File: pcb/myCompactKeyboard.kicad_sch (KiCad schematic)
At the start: 290 parts, among them J1 OLED_128x64, SW1 RotaryEncoder_Switch, SW2 RotaryEncoder_Switch, U1 Raspberry_Pi_Pico

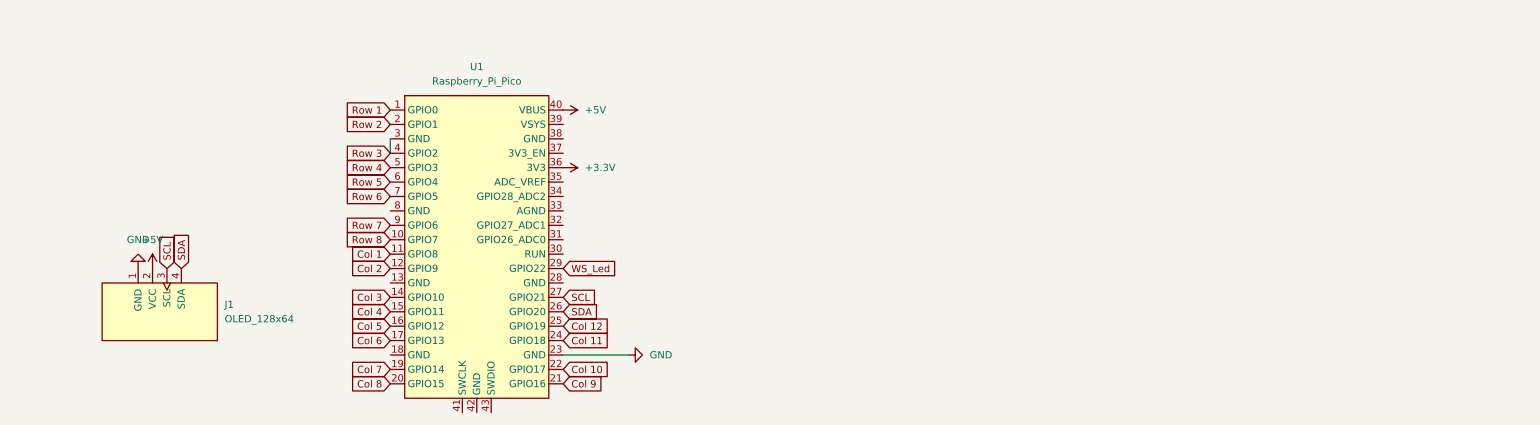
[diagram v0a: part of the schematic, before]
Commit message: added a jack conector
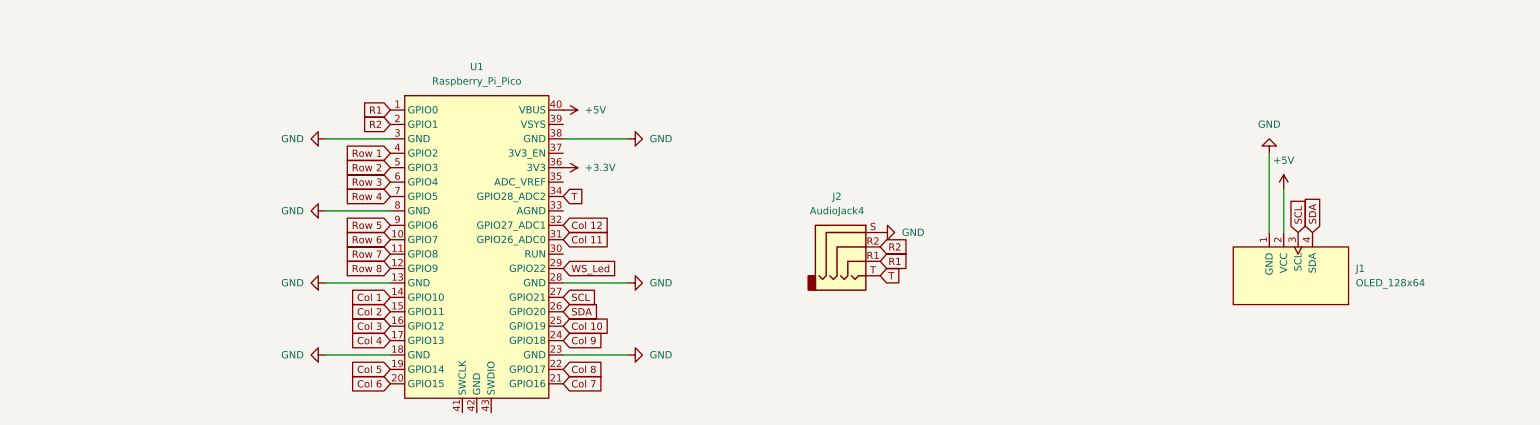
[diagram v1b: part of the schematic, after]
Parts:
- added J2: AudioJack4, symbol Connector_Audio:AudioJack4
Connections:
- net Col 1: now also U1.14 (GPIO10); no longer U1.11 (GPIO8)
- net Col 10: now also U1.25 (GPIO19); no longer U1.22 (GPIO17)
- net Col 11: now also U1.31 (GPIO26_ADC0); no longer U1.24 (GPIO18)
- net Col 12: now also U1.32 (GPIO27_ADC1); no longer U1.25 (GPIO19)
- net Col 2: now also U1.15 (GPIO11); no longer U1.12 (GPIO9)
- net Col 3: now also U1.16 (GPIO12); no longer U1.14 (GPIO10)
- net Col 4: now also U1.17 (GPIO13); no longer U1.15 (GPIO11)
- net Col 5: now also U1.19 (GPIO14); no longer U1.16 (GPIO12)
- net Col 6: now also U1.20 (GPIO15); no longer U1.17 (GPIO13)
- net Col 7: now also U1.21 (GPIO16); no longer U1.19 (GPIO14)
- net Col 8: now also U1.22 (GPIO17); no longer U1.20 (GPIO15)
- net Col 9: now also U1.24 (GPIO18); no longer U1.21 (GPIO16)
- net GND: now also U1.13 (GND), U1.18 (GND), U1.28 (GND), U1.3 (GND), U1.38 (GND), U1.8 (GND), J2.S
- net Row 1: now also U1.4 (GPIO2); no longer U1.1 (GPIO0)
- net Row 2: now also U1.5 (GPIO3); no longer U1.2 (GPIO1)
- net Row 3: now also U1.6 (GPIO4); no longer U1.3 (GND), U1.4 (GPIO2)
- net Row 4: now also U1.7 (GPIO5); no longer U1.5 (GPIO3)
- net Row 5: now also U1.9 (GPIO6); no longer U1.6 (GPIO4)
- net Row 6: now also U1.10 (GPIO7); no longer U1.7 (GPIO5)
- net Row 7: now also U1.11 (GPIO8); no longer U1.9 (GPIO6)
- net Row 8: now also U1.12 (GPIO9); no longer U1.10 (GPIO7)
- net T: now reaches U1.34 (GPIO28_ADC2)
- net T: now also J2.T
- new net R1: J2.R1, U1.1 (GPIO0)
- new net R2: J2.R2, U1.2 (GPIO1)
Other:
- moved on the sheet: J1

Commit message: wired all simple keyswitch connections
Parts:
- J2: footprint (none) -> Connector_Audio:Jack_3.5mm_CUI_SJ1-3524N_Horizontal
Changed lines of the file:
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@@
 			)
 		)
-		(property "Footprint" ""
+		(property "Footprint" "Connector_Audio:Jack_3.5mm_CUI_SJ1-3524N_Horizontal"
 			(at 227.33 308.61 0)
 			(effects

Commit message: changed jack to smd and fixed all errors and many warnings
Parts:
- J2: footprint Connector_Audio:Jack_3.5mm_CUI_SJ1-3524N_Horizontal -> Connector_Audio:Jack_3.5mm_CUI_SJ-3524-SMT_Horizontal
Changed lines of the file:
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@@
 			)
 		)
-		(property "Footprint" "Connector_Audio:Jack_3.5mm_CUI_SJ1-3524N_Horizontal"
+		(property "Footprint" "Connector_Audio:Jack_3.5mm_CUI_SJ-3524-SMT_Horizontal"
 			(at 227.33 308.61 0)
 			(effects

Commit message: added x.00u switches (instead of 1.00)
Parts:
- S54, S55: footprint ScottoKeebs_MX:MX_PCB_1.00u -> ScottoKeebs_MX:MX_PCB_3.00u
- S80: footprint ScottoKeebs_MX:MX_PCB_1.00u -> ScottoKeebs_MX:MX_PCB_2.00u_90deg
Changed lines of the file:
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@@
 			)
 		)
-		(property "Footprint" "ScottoKeebs_MX:MX_PCB_1.00u"
+		(property "Footprint" "ScottoKeebs_MX:MX_PCB_2.00u_90deg"
 			(at 129.54 231.14 0)
 			(effects
@@
 			)
 		)
-		(property "Footprint" "ScottoKeebs_MX:MX_PCB_1.00u"
+		(property "Footprint" "ScottoKeebs_MX:MX_PCB_3.00u"
 			(at 53.34 205.74 0)
 			(effects
@@
 			)
 		)
-		(property "Footprint" "ScottoKeebs_MX:MX_PCB_1.00u"
+		(property "Footprint" "ScottoKeebs_MX:MX_PCB_3.00u"
 			(at 53.34 180.34 0)
 			(effects

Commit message: moved half a row down top keys
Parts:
- S54, S55: footprint ScottoKeebs_MX:MX_PCB_3.00u -> ScottoKeebs_Scotto:MX_Hotswap_3.00u
- S80: footprint ScottoKeebs_MX:MX_PCB_2.00u_90deg -> ScottoKeebs_Scotto:MX_Hotswap_2.00u
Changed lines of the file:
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@@
 			)
 		)
-		(property "Footprint" "ScottoKeebs_MX:MX_PCB_2.00u_90deg"
+		(property "Footprint" "ScottoKeebs_Scotto:MX_Hotswap_2.00u"
 			(at 129.54 231.14 0)
 			(effects
@@
 			)
 		)
-		(property "Footprint" "ScottoKeebs_MX:MX_PCB_3.00u"
+		(property "Footprint" "ScottoKeebs_Scotto:MX_Hotswap_3.00u"
 			(at 53.34 205.74 0)
 			(effects
@@
 			)
 		)
-		(property "Footprint" "ScottoKeebs_MX:MX_PCB_3.00u"
+		(property "Footprint" "ScottoKeebs_Scotto:MX_Hotswap_3.00u"
 			(at 53.34 180.34 0)
 			(effects

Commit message: fixed hotswap keys and jack
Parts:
- S80: footprint ScottoKeebs_Scotto:MX_Hotswap_2.00u -> ScottoKeebs_Hotswap:Hotswap_MX_2.00u_90deg
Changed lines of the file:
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@@
 			)
 		)
-		(property "Footprint" "ScottoKeebs_Scotto:MX_Hotswap_2.00u"
+		(property "Footprint" "ScottoKeebs_Hotswap:Hotswap_MX_2.00u_90deg"
 			(at 129.54 231.14 0)
 			(effects

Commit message: converted firs spacebar to 2.75u and alt to 1.25u
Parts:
- S55: footprint ScottoKeebs_Scotto:MX_Hotswap_3.00u -> ScottoKeebs_Scotto:MX_Hotswap_2.75u
- S63: footprint ScottoKeebs_MX:MX_PCB_1.00u -> ScottoKeebs_MX:MX_PCB_1.25u
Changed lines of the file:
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@@
 			)
 		)
-		(property "Footprint" "ScottoKeebs_MX:MX_PCB_1.00u"
+		(property "Footprint" "ScottoKeebs_MX:MX_PCB_1.25u"
 			(at 78.74 205.74 0)
 			(effects
@@
 			)
 		)
-		(property "Footprint" "ScottoKeebs_Scotto:MX_Hotswap_3.00u"
+		(property "Footprint" "ScottoKeebs_Scotto:MX_Hotswap_2.75u"
 			(at 53.34 205.74 0)
 			(effects

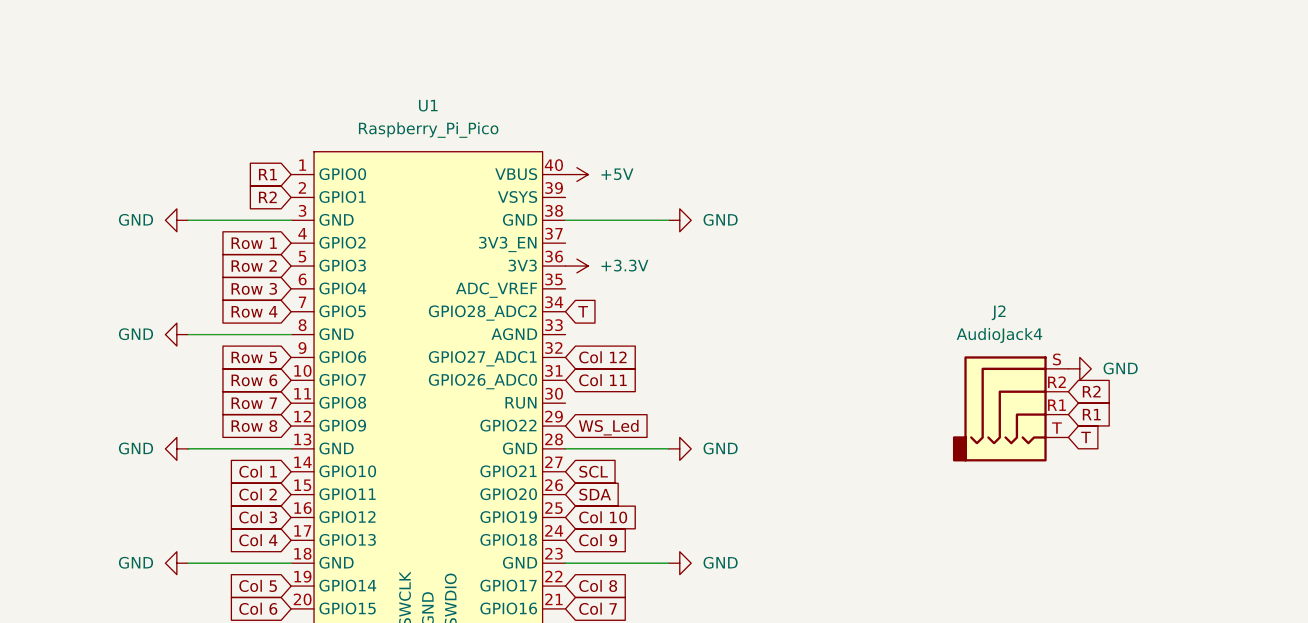
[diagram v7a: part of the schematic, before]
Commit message: remove jack and wire rotary encoders
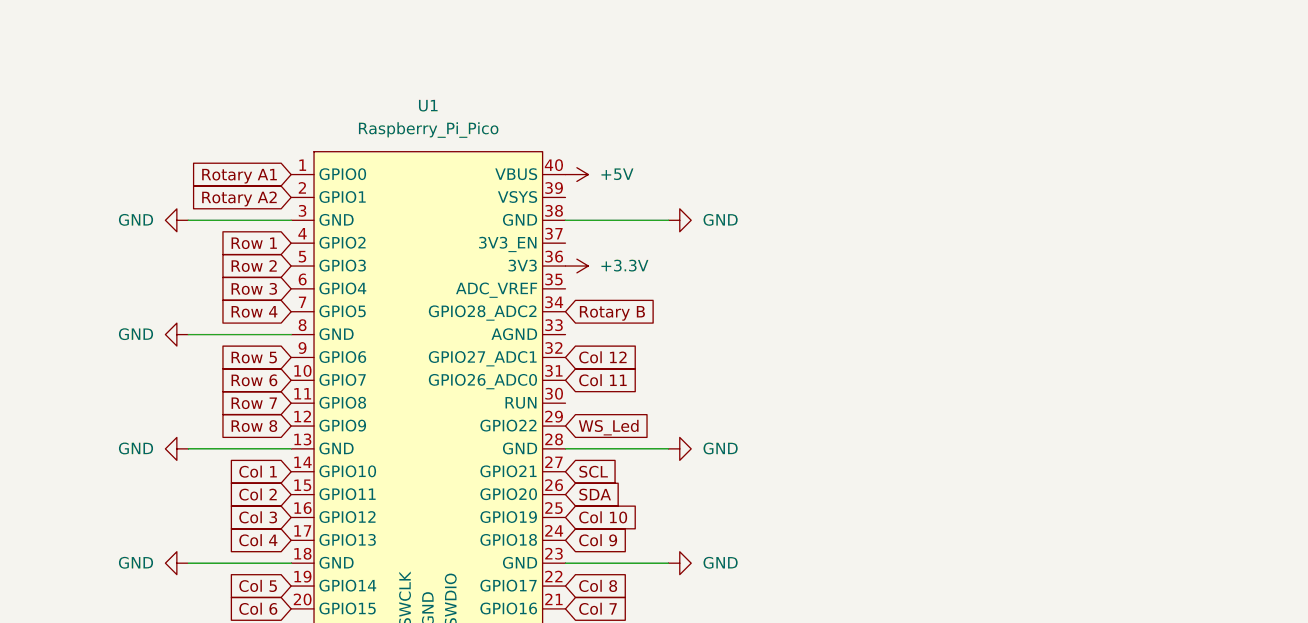
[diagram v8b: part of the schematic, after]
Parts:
- removed J2: AudioJack4, Connector_Audio:Jack_3.5mm_CUI_SJ-3524-SMT_Horizontal, symbol Connector_Audio:AudioJack4
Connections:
- net R1 is gone; now on net Rotary A1: U1.1 (GPIO0)
- net R2 is gone; now on net Rotary A2: U1.2 (GPIO1)
- net T is gone; now on net Rotary B: U1.34 (GPIO28_ADC2)
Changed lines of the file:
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@@
 		)
 	)
-	(global_label "T"
-		(shape input)
-		(at 232.41 313.69 0)
-		(fields_autoplaced yes)
-		(effects
-			(font
-				(size 1.27 1.27)
-			)
-			(justify left)
-		)
-		(property "Intersheetrefs" "${INTERSHEET_REFS}"
-			(at 236.3628 313.69 0)
-			(effects
-				(font
-					(size 1.27 1.27)
-				)
-				(justify left)
-				(hide yes)
-			)
-		)
-	)
-	(global_label "R1"
-		(shape input)
-		(at 146.05 284.48 180)
-		(fields_autoplaced yes)
-		(effects
-			(font
-				(size 1.27 1.27)
-			)
-			(justify right)
-		)
-		(property "Intersheetrefs" "${INTERSHEET_REFS}"
-			(at 140.5853 284.48 0)
-			(effects
-				(font
-					(size 1.27 1.27)
-				)
-				(justify right)
-				(hide yes)
-			)
-		)
-	)
 	(global_label "Col 8"
 		(shape input)
@@
 		)
 	)
-	(global_label "R2"
-		(shape input)
-		(at 146.05 287.02 180)
-		(fields_autoplaced yes)
-		(effects
-			(font
-				(size 1.27 1.27)
-			)
-			(justify right)
-		)
-		(property "Intersheetrefs" "${INTERSHEET_REFS}"
-			(at 140.5853 287.02 0)
-			(effects
-				(font
-					(size 1.27 1.27)
-				)
-				(justify right)
-				(hide yes)
-			)
-		)
-	)
 	(global_label "Col 1"
 		(shape input)
@@
 		)
 	)
-	(global_label "R2"
+	(global_label "Rotary A1"
 		(shape input)
-		(at 232.41 308.61 0)
+		(at 146.05 284.48 180)
 		(fields_autoplaced yes)
 		(effects
@@
 				(size 1.27 1.27)
 			)
-			(justify left)
+			(justify right)
 		)
 		(property "Intersheetrefs" "${INTERSHEET_REFS}"
-			(at 237.8747 308.61 0)
+			(at 133.7516 284.48 0)
 			(effects
 				(font
 					(size 1.27 1.27)
 				)
-				(justify left)
+				(justify right)
 				(hide yes)
 			)
@@
 		)
 	)
+	(global_label "Rotary A2"
+		(shape input)
+		(at 146.05 287.02 180)
+		(fields_autoplaced yes)
+		(effects
+			(font
+				(size 1.27 1.27)
+			)
+			(justify right)
+		)
+		(property "Intersheetrefs" "${INTERSHEET_REFS}"
+			(at 133.7516 287.02 0)
+			(effects
+				(font
+					(size 1.27 1.27)
+				)
+				(justify right)
+				(hide yes)
+			)
+		)
+	)
 	(global_label "Col 8"
 		(shape input)
@@
 		)
 	)
-	(global_label "T"
+	(global_label "WS_Led"
 		(shape input)
-		(at 176.53 299.72 0)
+		(at 276.86 25.4 180)
 		(fields_autoplaced yes)
 		(effects
@@
 				(size 1.27 1.27)
 			)
-			(justify left)
+			(justify right)
 		)
 		(property "Intersheetrefs" "${INTERSHEET_REFS}"
-			(at 180.4828 299.72 0)
+			(at 266.9806 25.4 0)
 			(effects
 				(font
 					(size 1.27 1.27)
 				)
-				(justify left)
+				(justify right)
 				(hide yes)
 			)
 		)
 	)
-	(global_label "WS_Led"
+	(global_label "Rotary B"
 		(shape input)
-		(at 276.86 25.4 180)
+		(at 176.53 299.72 0)
 		(fields_autoplaced yes)
 		(effects
@@
 				(size 1.27 1.27)
 			)
-			(justify right)
+			(justify left)
 		)
 		(property "Intersheetrefs" "${INTERSHEET_REFS}"
-			(at 266.9806 25.4 0)
+			(at 187.8003 299.72 0)
 			(effects
 				(font
 					(size 1.27 1.27)
 				)
-				(justify right)
+				(justify left)
 				(hide yes)
 			)
@@
 		)
 	)
-	(global_label "R1"
-		(shape input)
-		(at 232.41 311.15 0)
-		(fields_autoplaced yes)
-		(effects
-			(font
-				(size 1.27 1.27)
-			)
-			(justify left)
-		)
-		(property "Intersheetrefs" "${INTERSHEET_REFS}"
-			(at 237.8747 311.15 0)
-			(effects
-				(font
-					(size 1.27 1.27)
-				)
-				(justify left)
-				(hide yes)
-			)
-		)
-	)
 	(global_label "Row 4"
 		(shape input)
@@
 	)
 	(symbol
-		(lib_id "power:GND")
-		(at 232.41 306.07 90)
-		(unit 1)
-		(exclude_from_sim no)
-		(in_bom yes)
-		(on_board yes)
-		(dnp no)
-		(fields_autoplaced yes)
-		(property "Reference" "#PWR012"
-			(at 238.76 306.07 0)
-			(effects
-				(font
-					(size 1.27 1.27)
-				)
-				(hide yes)
-			)
-		)
-		(property "Value" "GND"
-			(at 236.22 306.0699 90)
-			(effects
-				(font
-					(size 1.27 1.27)
-				)
-				(justify right)
-			)
-		)
-		(property "Footprint" ""
-			(at 232.41 306.07 0)
-			(effects
-				(font
-					(size 1.27 1.27)
-				)
-				(hide yes)
-			)
-		)
-		(property "Datasheet" ""
-			(at 232.41 306.07 0)
-			(effects
-				(font
-					(size 1.27 1.27)
-				)
-				(hide yes)
-			)
-		)
-		(property "Description" "Power symbol creates a global label with name \"GND\" , ground"
-			(at 232.41 306.07 0)
-			(effects
-				(font
-					(size 1.27 1.27)
-				)
-				(hide yes)
-			)
-		)
-		(pin "1"
-		)
-		(instances
-			(project ""
-				(path "/a5f71a14-17d5-4701-ba70-d64b25a756b2"
-					(reference "#PWR012")
-					(unit 1)
-				)
-			)
-		)
-	)
-	(symbol
 		(lib_id "ScottoKeebs:Placeholder_Diode")
 		(at 68.58 85.09 90)
@@
 					(unit 1)
 				)
-			)
-		)
-	)
-	(symbol
-		(lib_id "Connector_Audio:AudioJack4")
-		(at 227.33 308.61 0)
-		(unit 1)
-		(exclude_from_sim no)
-		(in_bom yes)
-		(on_board yes)
-		(dnp no)
-		(fields_autoplaced yes)
-		(property "Reference" "J2"
-			(at 224.79 299.72 0)
-			(effects
-				(font
-					(size 1.27 1.27)
-				)
-			)
-		)
-		(property "Value" "AudioJack4"
-			(at 224.79 302.26 0)
-			(effects
-				(font
-					(size 1.27 1.27)
-				)
-			)
-		)
-		(property "Footprint" "Connector_Audio:Jack_3.5mm_CUI_SJ-3524-SMT_Horizontal"
-			(at 227.33 308.61 0)
-			(effects
-				(font
-					(size 1.27 1.27)
-				)
-				(hide yes)
-			)
-		)
-		(property "Datasheet" "~"
-			(at 227.33 308.61 0)
-			(effects
-				(font
-					(size 1.27 1.27)
-				)
-				(hide yes)
-			)
-		)
-		(property "Description" "Audio Jack, 4 Poles (TRRS)"
-			(at 227.33 308.61 0)
-			(effects
-				(font
-					(size 1.27 1.27)
-				)
-				(hide yes)
-			)
-		)
-		(pin "R2"
-		)
-		(pin "R1"
-		)
-		(pin "S"
-		)
-		(pin "T"
-		)
-		(instances
-			(project ""
-				(path "/a5f71a14-17d5-4701-ba70-d64b25a756b2"
-					(reference "J2")
-					(unit 1)
-				)
